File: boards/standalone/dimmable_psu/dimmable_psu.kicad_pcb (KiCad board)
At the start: 2 copper layers, 100 x 50 mm, 81 parts, among them J1 DIM_IN, J2 PWM_IN, J3 POWER, J4 POWER_OUT, Q1 2N7002, Q2 IRF540N, Q3 IRF540N, SW1 SW_DIP_SPLIT_x02, U1 LM324, U2 LMC7660, U3 TPS92640

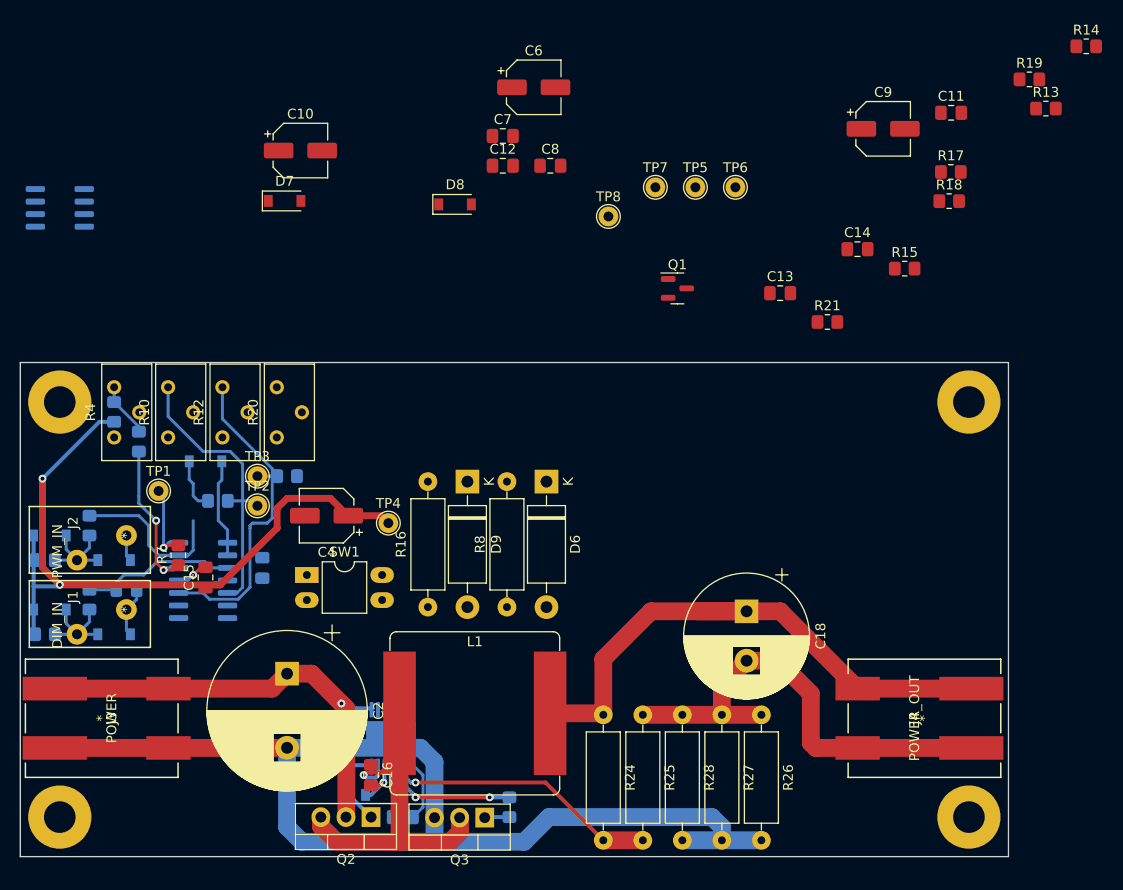
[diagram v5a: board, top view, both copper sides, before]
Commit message: some more work on dimmable psu pcb
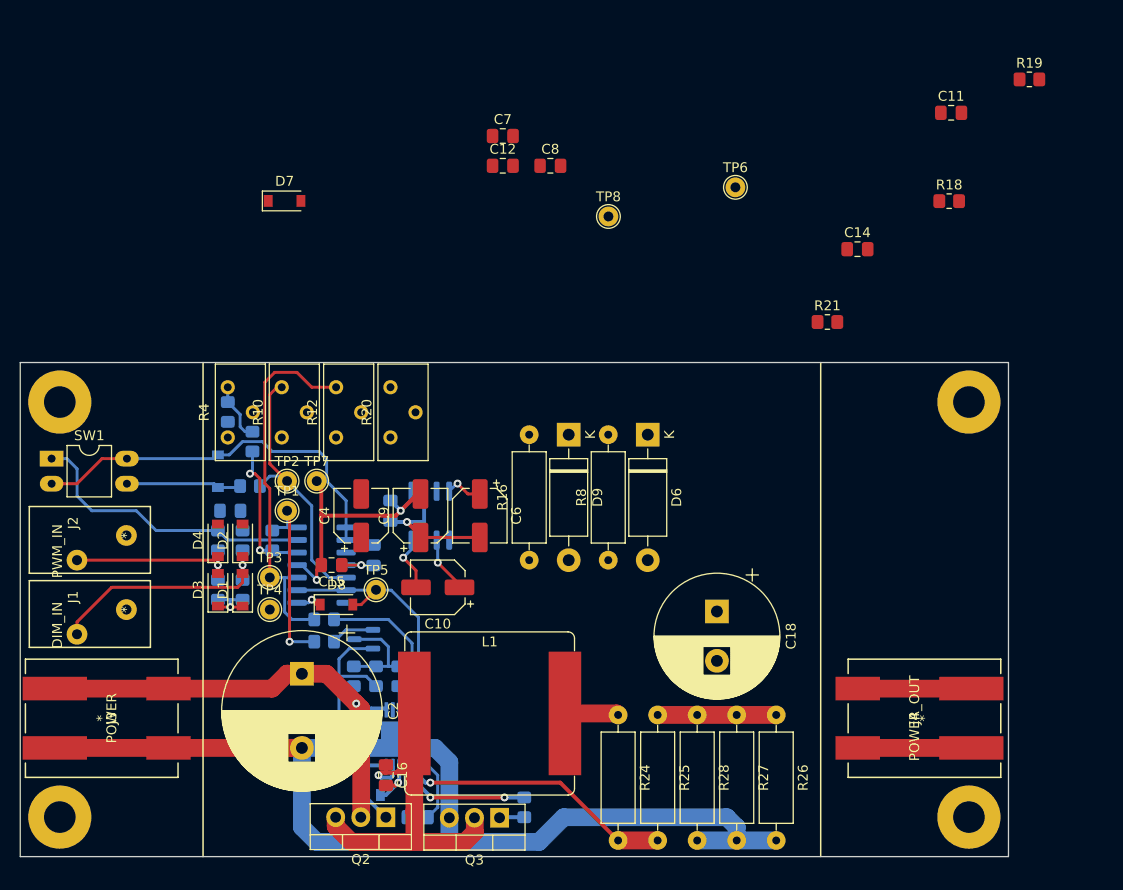
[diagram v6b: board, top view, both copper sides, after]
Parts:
- C13, Q1, R13, R14, R15, R17, R7: moved to B.Cu
- D1, D2, D3, D4: moved to F.Cu
- moved R14 97.8 mm to (33.8, 31.8), turned to 90 degrees
- moved R13 90.8 mm to (30.8, 28.2)
- moved R17 75.7 mm to (38.2, 31.8), turned to -90 degrees
- moved R15 67.6 mm to (36.0, 31.8), turned to -90 degrees
- moved C9 61.0 mm to (40.5, 15.5), turned to 90 degrees
- moved TP5 52.0 mm to (36.0, 23.0)
- moved U2 48.8 mm to (41.5, 15.5), turned to 90 degrees
- moved Q1 47.6 mm to (34.8, 28.0), turned to 180 degrees
- moved C10 46.3 mm to (42.2, 22.8), turned to 180 degrees
- moved TP7 45.4 mm to (30.0, 12.0)
- moved C13 45.2 mm to (37.5, 15.0), turned to -90 degrees
- moved C6 43.7 mm to (46.5, 15.5), turned to -90 degrees
- moved D8 42.2 mm to (32.0, 24.5)
- moved SW1 28.4 mm to (3.17, 9.72)
- moved R29 20.5 mm to (22.5, 23.0), turned to 90 degrees
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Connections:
- net Net-(C6-Pad1) renamed /VNEGREF
- SW1 pad 3: Net-(D5-Pad2) -> Net-(D5-Pad1)
- SW1 pad 4: Net-(D5-Pad1) -> Net-(D5-Pad2)
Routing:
- net VDD: track 72.5 -> 10.6 mm
- net /OUT+: track 59.2 -> 17.6 mm
- net Net-(D5-Pad2): track 10.0 -> 39.3 mm
- net GND: track 126.2 -> 155.5 mm, vias 0 -> 1
- net /IADJ: track 0.00 -> 25.7 mm
- net -VSW: track 3.28 -> 27.8 mm, vias 1 -> 2
- net /OUT-: track 47.8 -> 23.5 mm
- net Net-(C1-Pad1): track 16.3 -> 0.00 mm
- net /VREF: track 0.00 -> 15.6 mm
- net /DIM_IN: track 10.3 -> 25.3 mm, vias 0 -> 1
- net Net-(R6-Pad2): track 16.6 -> 29.9 mm
- net Net-(R13-Pad1): track 9.30 -> 20.7 mm
- net /UDIM_OFF: track 0.00 -> 10.2 mm
- net /PWM_IN: track 10.3 -> 19.1 mm, vias 0 -> 1
- net Net-(D5-Pad1): track 5.37 -> 11.7 mm
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
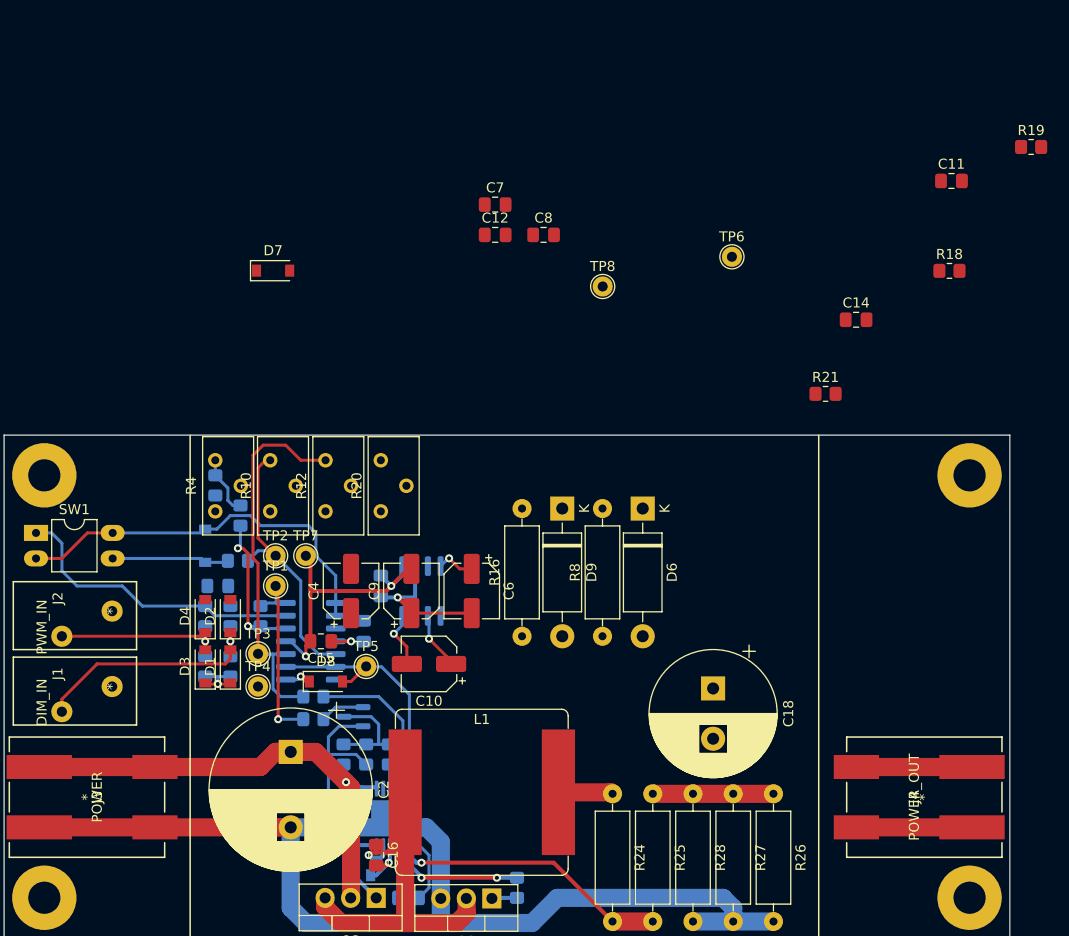
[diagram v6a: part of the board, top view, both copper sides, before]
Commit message: rework dimmable_psu opamp power supplies
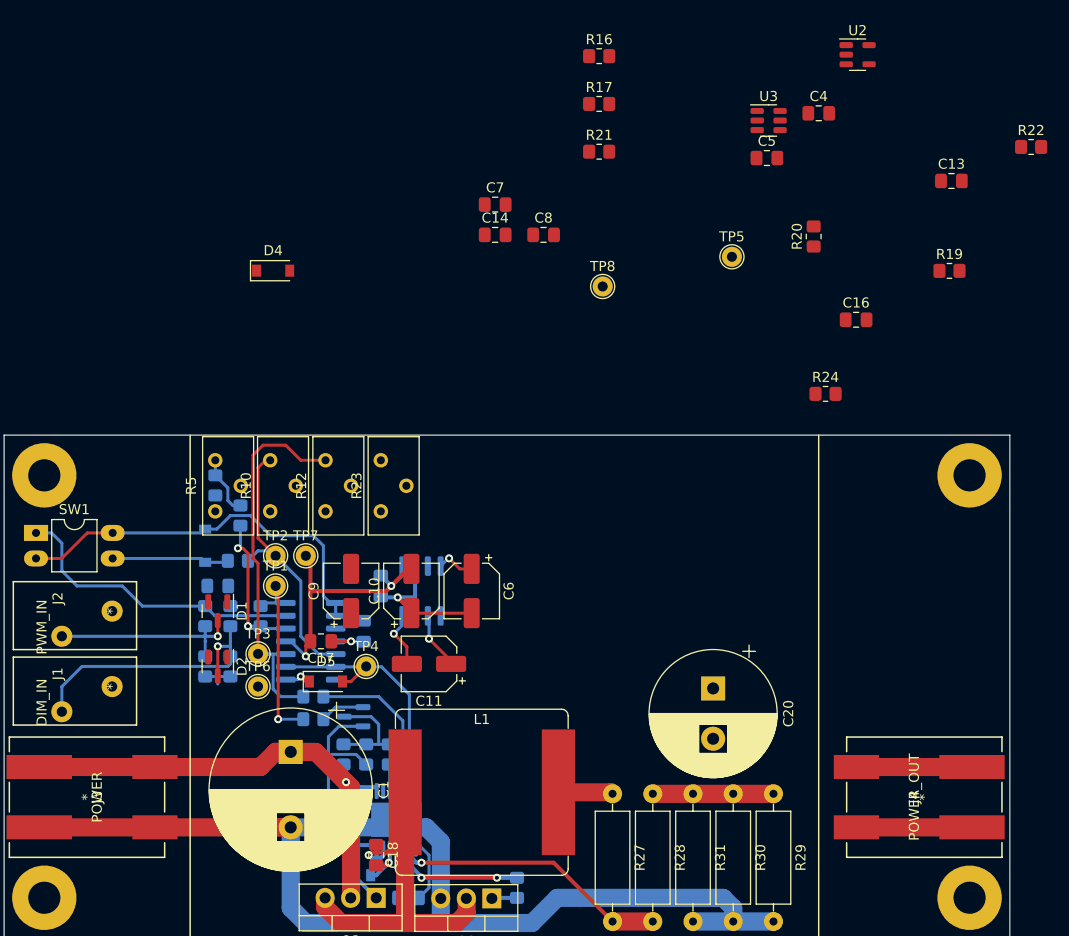
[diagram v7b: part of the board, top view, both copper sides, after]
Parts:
- removed the D3 at (20.0, 23.0)
- removed the D4 at (20.0, 18.0)
- removed the D6 at (63.5, 7.30)
- removed D9: 2.7v, Diode_THT:D_DO-15_P12.70mm_Horizontal
- added C4: 100n, Capacitor_SMD:C_0805_2012Metric_Pad1.18x1.45mm_HandSolder, F.Cu at (81.0, -32.0)
- added C5: 100n, Capacitor_SMD:C_0805_2012Metric_Pad1.18x1.45mm_HandSolder, F.Cu at (75.8, -27.6)
- added R17: 47k, Resistor_SMD:R_0805_2012Metric_Pad1.20x1.40mm_HandSolder, F.Cu at (59.2, -32.9)
- added R21: 59k, Resistor_SMD:R_0805_2012Metric_Pad1.20x1.40mm_HandSolder, F.Cu at (59.2, -28.2)
- added U2: AP2205-ADJ, Package_TO_SOT_SMD:SOT-23-5, F.Cu at (84.9, -37.8)
- added U5: TPS92640, Package_SO:HTSSOP-14-1EP_4.4x5mm_P0.65mm_EP3.4x5mm_Mask3x3.1mm, B.Cu at (39.0, 38.2)
- D1, D2: value D_Schottky_Trans -> BAT54S; footprint Diode_SMD:D_SOD-123 -> Package_TO_SOT_SMD:SOT-23
- R16: value 1.2k -> 47k; footprint Resistor_THT:R_Axial_DIN0309_L9.0mm_D3.2mm_P12.70mm_Horizontal -> Resistor_SMD:R_0805_2012Metric_Pad1.20x1.40mm_HandSolder
- R2: renamed from R1; value 47k -> 22k
- R20: renamed from R8; value 750 -> 1.5M; footprint Resistor_THT:R_Axial_DIN0309_L9.0mm_D3.2mm_P12.70mm_Horizontal -> Resistor_SMD:R_0805_2012Metric_Pad1.20x1.40mm_HandSolder
- U3: value TPS92640 -> MAX17651; footprint Package_SO:HTSSOP-14-1EP_4.4x5mm_P0.65mm_EP3.4x5mm_Mask3x3.1mm -> Package_TO_SOT_SMD:TSOT-23-6; moved to F.Cu
- moved U3 78.6 mm to (76.0, -31.3), turned to 0 degrees
- moved R16 58.2 mm to (59.2, -37.7), turned to 0 degrees
- moved R20 45.0 mm to (80.5, -19.8)
- moved D1 5.64 mm to (21.2, 17.5), turned to -90 degrees
- moved D2 5.15 mm to (21.2, 23.0), turned to -90 degrees
- renumbered C2 to C1, C9 to C10, C10 to C11, C5 to C12, C11 to C13, C12 to C14, C13 to C15, C14 to C16, C15 to C17, C16 to C18, C17 to C19, C3 to C2, C18 to C20, C1 to C3, C4 to C9, D5 to D3, D7 to D4, D8 to D5, D10 to D6, R29 to R1, R17 to R18, R18 to R19, R19 to R22, R20 to R23, R21 to R24, R22 to R25, R23 to R26, R24 to R27, R25 to R28, R26 to R29, R2 to R3, R27 to R30, R28 to R31, R3 to R4, R4 to R5, R5 to R6, R6 to R7, R7 to R8, TP5 to TP4, TP6 to TP5, TP4 to TP6, U2 to U4
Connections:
- C13 pad 1: Net-(C11-Pad1) (its old number) -> Net-(C13-Pad1)
- C16 pad 1: Net-(C14-Pad1) -> Net-(C16-Pad1)
- C18 pad 2: Net-(C16-Pad2) -> Net-(C18-Pad2)
- C19 pad 1: Net-(C17-Pad1) -> Net-(C19-Pad1)
- D1 pad 1: VDD -> GND
- D1 pad 2: /DIM_IN -> VDD
- D2 pad 1: /DIM_IN -> GND
- D2 pad 2: GND -> VDD
- D6 pad 1: Net-(C16-Pad2) -> Net-(C18-Pad2)
- D6 pad 2: Net-(C17-Pad1) -> Net-(C19-Pad1)
- R16 pad 1: VPP -> /VNEGREF
- R16 pad 2: /VNEGREF -> Net-(R16-Pad2)
- R20 pad 1: VPP -> VDD
- R20 pad 2: VDD -> Net-(R20-Pad2)
- R24 pad 2: Net-(C11-Pad1) (its old number) -> Net-(C13-Pad1)
- R25 pad 1: Net-(R22-Pad1) -> Net-(R25-Pad1)
- R26 pad 1: Net-(R23-Pad1) -> Net-(R26-Pad1)
- U3 pad 2: Net-(C11-Pad1) (its old number) -> GND
- U3 pad 3: /UDIM -> VPP
- U3 pad 4: /VOUT_SENSE -> VDD
- U3 pad 5: /VREF -> unconnected-(U3-Pad5)
- U3 pad 6: /IADJ -> Net-(R20-Pad2)
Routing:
- net Net-(R26-Pad1): track 0.00 -> 13.4 mm, vias 0 -> 2
- net Net-(R23-Pad1): track 13.4 -> 0.00 mm, vias 2 -> 0
- net Net-(C19-Pad1): track 0.00 -> 5.69 mm
- net Net-(C17-Pad1): track 5.69 -> 0.00 mm
- net Net-(C18-Pad2): track 0.00 -> 5.37 mm, vias 0 -> 1
- net Net-(C16-Pad2): track 5.37 -> 0.00 mm, vias 1 -> 0
- net /DIM_IN: track 25.3 -> 28.2 mm
- net Net-(R25-Pad1): track 0.00 -> 2.91 mm
- net Net-(R22-Pad1): track 2.91 -> 0.00 mm
- net VDD: track 10.6 -> 8.00 mm, vias 2 -> 1
- net /PWM_IN: track 19.1 -> 19.7 mm

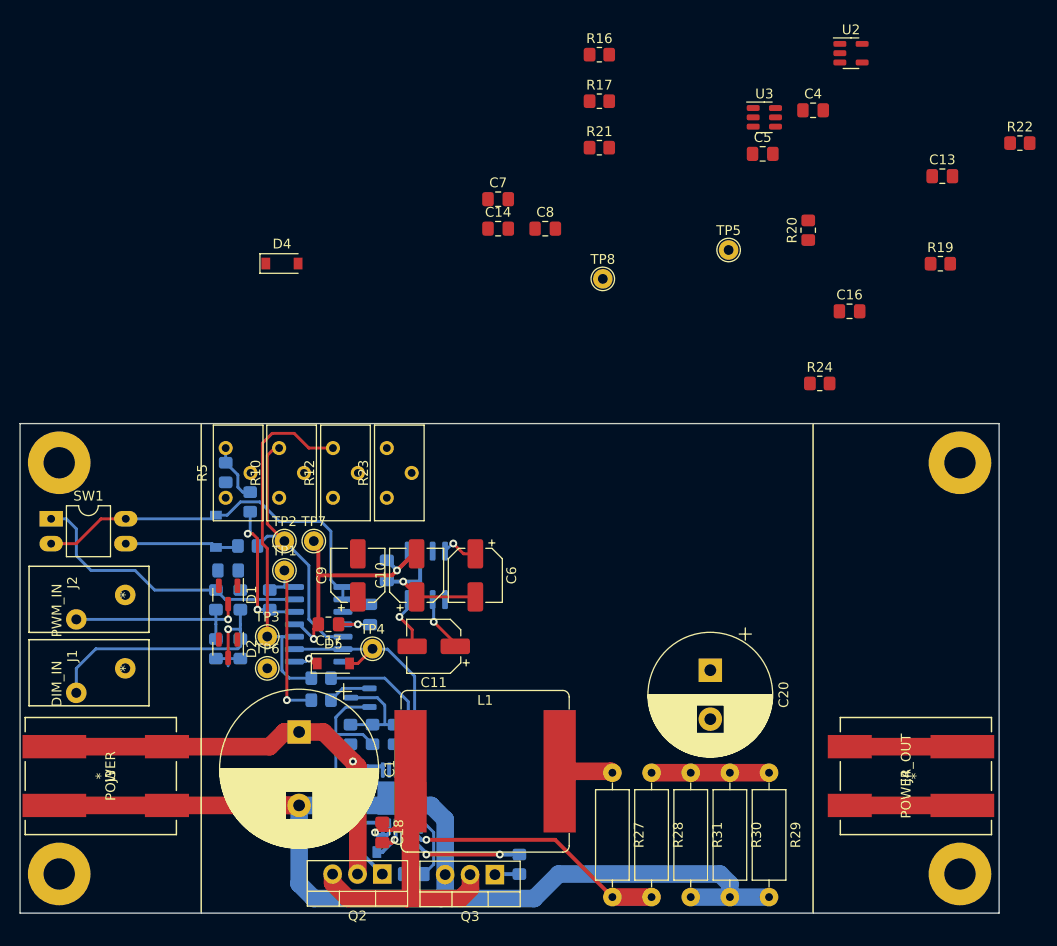
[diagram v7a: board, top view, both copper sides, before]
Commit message: dimmable psu pcb almost finished
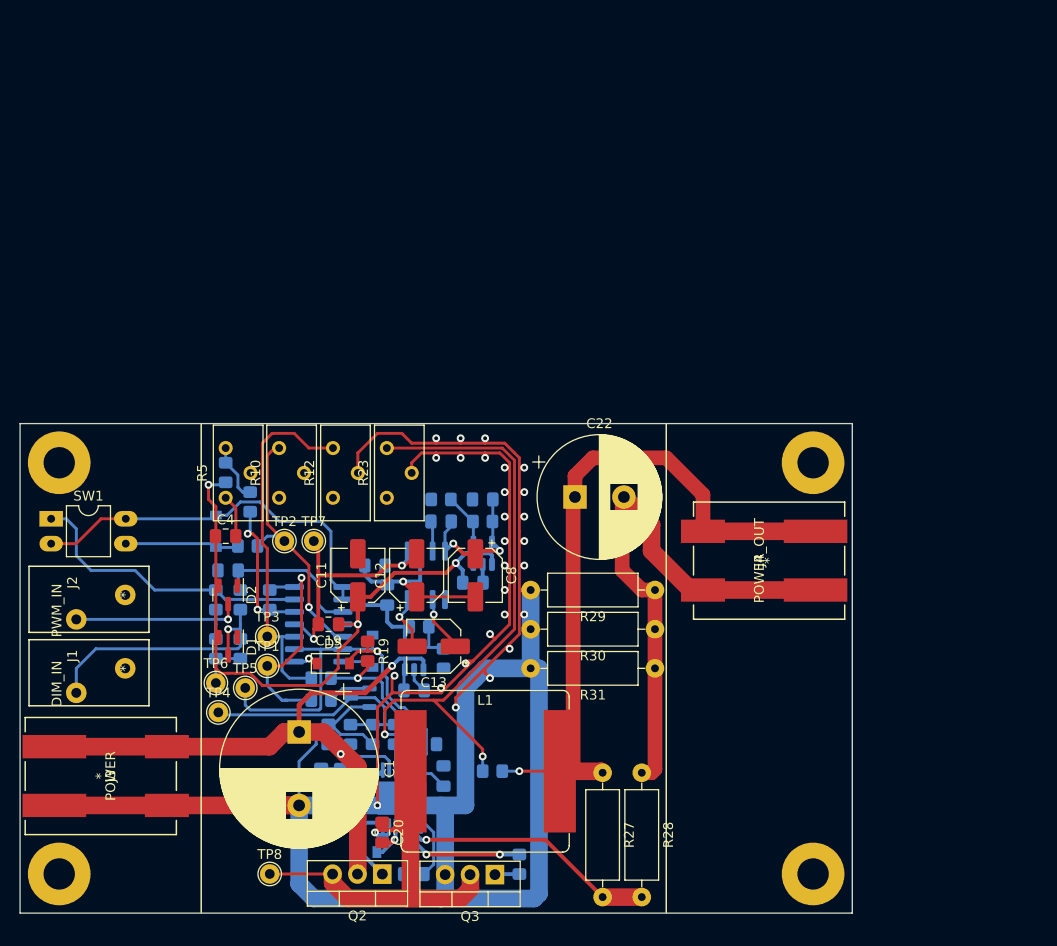
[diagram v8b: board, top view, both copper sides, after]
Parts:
- added C3: 100n, Capacitor_SMD:C_0805_2012Metric_Pad1.18x1.45mm_HandSolder, B.Cu at (31.5, 31.8)
- added C4: 100n, Capacitor_SMD:C_0805_2012Metric_Pad1.18x1.45mm_HandSolder, F.Cu at (21.0, 11.5)
- C10: renamed from C8; moved to B.Cu
- C15: renamed from C13; moved to B.Cu
- C16: renamed from C14; moved to B.Cu
- C18: renamed from C16; moved to B.Cu
- C6: renamed from C4; moved to B.Cu
- C7: renamed from C5; moved to B.Cu
- C9: renamed from C7; moved to B.Cu
- D4, R16, R17, R20, R21, R22, R24, U2, U3: moved to B.Cu
- moved C15 88.4 mm to (30.8, 36.2), turned to -90 degrees
- moved R22 83.8 mm to (48.2, 35.5), turned to 180 degrees
- moved R19 70.6 mm to (35.5, 23.2), turned to -90 degrees
- moved TP4 70.3 mm to (20.2, 29.5)
- moved TP8 69.7 mm to (25.5, 46.0)
- moved U3 65.8 mm to (40.2, 24.0), turned to 90 degrees
- moved C7 65.3 mm to (40.2, 27.2)
- moved U2 63.4 mm to (47.2, 13.2), turned to 90 degrees
- moved R24 63.4 mm to (32.8, 36.2), turned to 90 degrees
- moved C18 63.0 mm to (43.2, 36.0), turned to 90 degrees
- moved C6 59.5 mm to (46.2, 16.2)
- moved R20 56.7 mm to (40.8, 20.8), turned to 0 degrees
- moved R21 54.6 mm to (43.2, 24.0), turned to -90 degrees
- moved C16 53.2 mm to (41.5, 32.8)
- moved R16 49.1 mm to (47.2, 10.0), turned to 180 degrees
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- renumbered C9 to C11, C10 to C12, C11 to C13, C12 to C14, C15 to C17, C17 to C19, C18 to C20, C19 to C21, C20 to C22, C3 to C5, C6 to C8, TP5 to TP4, TP4 to TP5
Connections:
- TP4 pad 1: /UDIM -> /UDIM_OFF
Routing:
- net GND: track 155.5 -> 316.9 mm, vias 1 -> 28
- net VDD: track 8.00 -> 84.0 mm, vias 1 -> 3
- net /VOUT_SENSE: track 0.00 -> 65.2 mm, vias 0 -> 2
- net /OUT+: track 17.6 -> 71.8 mm, vias 0 -> 1
- net /OUT-: track 23.5 -> 56.6 mm
- net VPP: track 50.9 -> 75.6 mm, vias 1 -> 3
- net /IADJ: track 25.7 -> 45.7 mm, vias 0 -> 1
- net Net-(C5-Pad1): track 0.00 -> 15.8 mm
- net /UDIM_OFF: track 10.2 -> 24.5 mm
- net /VNEGREF: track 3.85 -> 14.9 mm, vias 1 -> 2
- net Net-(C15-Pad1): track 0.00 -> 8.61 mm
- net /POWER_JUN: track 42.7 -> 49.1 mm
- net Net-(R16-Pad2): track 0.00 -> 5.32 mm
- net Net-(R20-Pad2): track 0.00 -> 4.11 mm
- net Net-(D4-Pad1): track 0.00 -> 3.27 mm
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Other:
- board size 100 x 50 mm -> 85 x 50 mm
